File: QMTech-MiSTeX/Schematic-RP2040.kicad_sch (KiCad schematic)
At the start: 24 parts, among them J9 Conn_01x02, U1 W25Q128JVS, U2 RP2040, X1 X322512MSB4SI

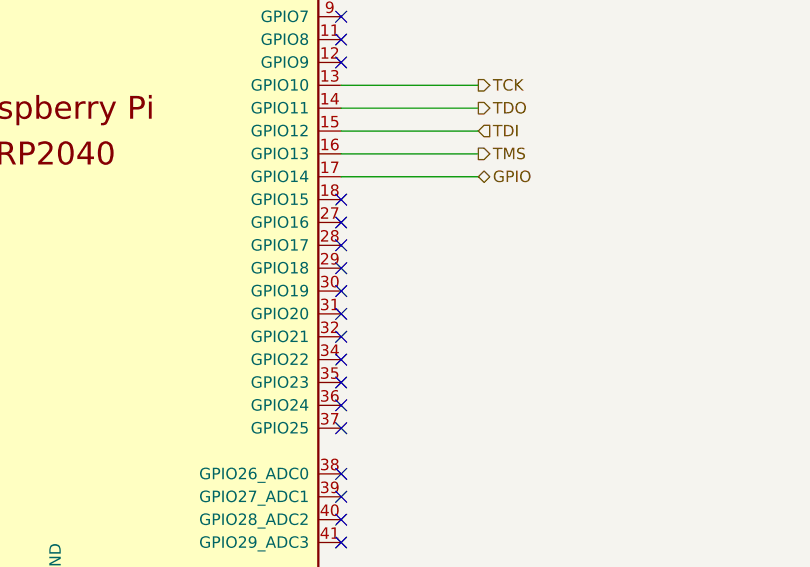
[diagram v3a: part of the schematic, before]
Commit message: add a power switch and break out and break out 4 more GPIOs on RP2040
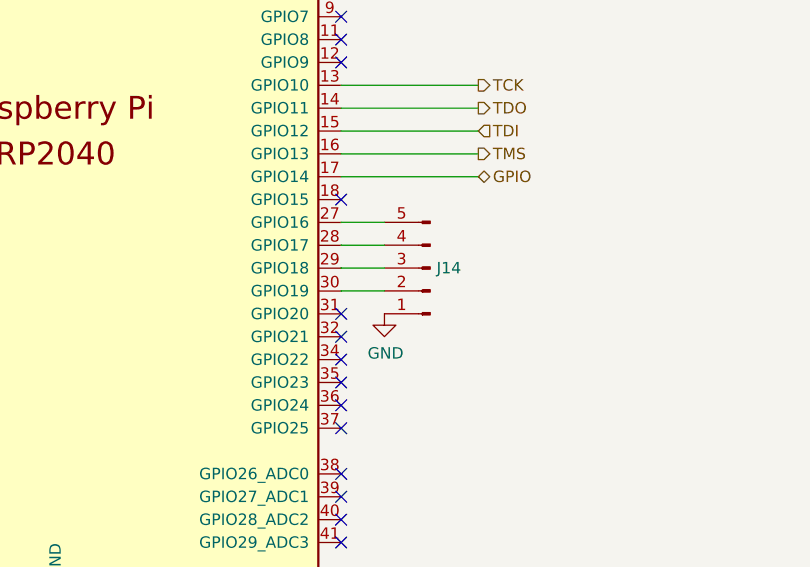
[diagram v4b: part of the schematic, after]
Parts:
- added J14: Conn_01x05_Pin, Connector_PinHeader_2.54mm:PinHeader_1x05_P2.54mm_Vertical, symbol Connector:Conn_01x05_Pin
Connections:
- net GND: now also J14.1 (Pin_1)
- net at U2.27 (GPIO16): now also J14.5 (Pin_5)
- net at U2.28 (GPIO17): now also J14.4 (Pin_4)
- net at U2.29 (GPIO18): now also J14.3 (Pin_3)
- net at U2.30 (GPIO19): now also J14.2 (Pin_2)
- no-connect marks 23 -> 19
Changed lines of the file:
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@@
   )
   (no_connect (at 186.4106 79.5782))
-  (no_connect (at 186.4106 117.6782))
   (no_connect (at 186.4106 89.7382))
   (no_connect (at 186.4106 92.2782))
@@
   (no_connect (at 186.4106 87.1982))
   (no_connect (at 186.4106 130.3782))
-  (no_connect (at 186.4106 120.2182))
-  (no_connect (at 186.4106 112.5982))
   (no_connect (at 186.4106 148.1582))
   (no_connect (at 186.4106 84.6582))
@@
   (no_connect (at 186.4106 143.0782))
   (no_connect (at 186.4106 110.0582))
-  (no_connect (at 186.4106 115.1382))
   (no_connect (at 186.4106 140.5382))
   (no_connect (at 186.4106 122.7582))
@@
     (stroke (width 0) (type default))
   )
+  (wire (pts (xy 191.2175 115.1242) (xy 186.4246 115.1242))
+    (stroke (width 0) (type default))
+  )
   (wire (pts (xy 237.2106 30.0482) (xy 225.7806 30.0482))
     (stroke (width 0) (type default))
@@
     (stroke (width 0) (type default))
   )
+  (wire (pts (xy 191.2175 117.6642) (xy 186.4246 117.6642))
+    (stroke (width 0) (type default))
+  )
+  (wire (pts (xy 186.4246 115.1242) (xy 186.4106 115.1382))
+    (stroke (width 0) (type default))
+  )
   (wire (pts (xy 202.9206 22.4282) (xy 202.9206 21.1582))
     (stroke (width 0) (type default))
@@
     (stroke (width 0) (type default))
   )
+  (wire (pts (xy 191.2175 120.2042) (xy 186.4246 120.2042))
+    (stroke (width 0) (type default))
+  )
   (wire (pts (xy 26.0096 84.0232) (xy 27.2796 84.0232))
     (stroke (width 0) (type default))
@@
     (stroke (width 0) (type default))
   )
+  (wire (pts (xy 186.4246 112.5842) (xy 186.4106 112.5982))
+    (stroke (width 0) (type default))
+  )
   (wire (pts (xy 122.9106 139.2682) (xy 108.9406 139.2682))
     (stroke (width 0) (type default))
@@
     (stroke (width 0) (type default))
   )
+  (wire (pts (xy 186.4246 120.2042) (xy 186.4106 120.2182))
+    (stroke (width 0) (type default))
+  )
   (wire (pts (xy 70.7136 113.3602) (xy 92.4306 113.3602))
     (stroke (width 0) (type default))
@@
     (stroke (width 0) (type default))
   )
+  (wire (pts (xy 186.4246 117.6642) (xy 186.4106 117.6782))
+    (stroke (width 0) (type default))
+  )
   (wire (pts (xy 49.2506 130.7592) (xy 53.4861 130.7592))
     (stroke (width 0) (type default))
@@
     (stroke (width 0) (type default))
   )
+  (wire (pts (xy 191.2175 112.5842) (xy 186.4246 112.5842))
+    (stroke (width 0) (type default))
+  )
   (wire (pts (xy 114.0206 22.4282) (xy 114.0206 21.1582))
     (stroke (width 0) (type default))
@@
     )
   )
+  (symbol (lib_id "power:GND") (at 191.2175 122.7442 0) (unit 1)
+    (in_bom yes) (on_board yes) (dnp no)
+    (property "Reference" "#PWR0154" (at 191.2175 129.0942 0)
+      (effects (font (size 1.27 1.27)) hide)
+    )
+    (property "Value" "GND" (at 191.3445 127.1384 0)
+      (effects (font (size 1.27 1.27)))
+    )
+    (property "Footprint" "" (at 191.2175 122.7442 0)
+      (effects (font (size 1.27 1.27)) hide)
+    )
+    (property "Datasheet" "" (at 191.2175 122.7442 0)
+      (effects (font (size 1.27 1.27)) hide)
+    )
+    (pin "1")
+    (instances
+      (project "QMTech-MiSTeX"
+        (path "/bf95850e-2fcb-4784-a603-f17fc357556b/6eb28fc4-fd96-4fb7-b136-67141c56dbda"
+          (reference "#PWR0154") (unit 1)
+        )
+      )
+    )
+  )
   (symbol (lib_id "jlcpcb-basic-mlcc-0402:100nF") (at 125.4506 24.9682 0) (unit 1)
     (in_bom yes) (on_board yes) (dnp no)
@@
         )
       )
+    )
+  )
+  (symbol (lib_id "Connector:Conn_01x05_Pin") (at 196.2975 117.6642 180) (unit 1)
+    (in_bom yes) (on_board yes) (dnp no) (fields_autoplaced)
+    (property "Reference" "J14" (at 197.0087 117.6642 0)
+      (effects (font (size 1.27 1.27)) (justify right))
+    )
+    (property "Value" "Conn_01x05_Pin" (at 197.0087 118.8763 0)
+      (effects (font (size 1.27 1.27)) (justify right) hide)
+    )
+    (property "Footprint" "Connector_PinHeader_2.54mm:PinHeader_1x05_P2.54mm_Vertical" (at 196.2975 117.6642 0)
+      (effects (font (size 1.27 1.27)) hide)
+    )
+    (property "Datasheet" "~" (at 196.2975 117.6642 0)
+      (effects (font (size 1.27 1.27)) hide)
+    )
+    (pin "2")
+    (pin "4")
+    (pin "3")
+    (pin "5")
+    (pin "1")
+    (instances
+      (project "QMTech-MiSTeX"
+        (path "/bf95850e-2fcb-4784-a603-f17fc357556b/6eb28fc4-fd96-4fb7-b136-67141c56dbda"
+          (reference "J14") (unit 1)
+        )
+      )

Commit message: silkscreen, schematic titles
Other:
- title: (none) -> RP2040 JTAG Programmer
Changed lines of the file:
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@@
 (kicad_sch (version 20230121) (generator eeschema)
   (paper "A4")
+  (title_block
+    (title "RP2040 JTAG Programmer")
+  )
   (junction (at 171.1706 36.3982) (diameter 0) (color 0 0 0 0)
   )

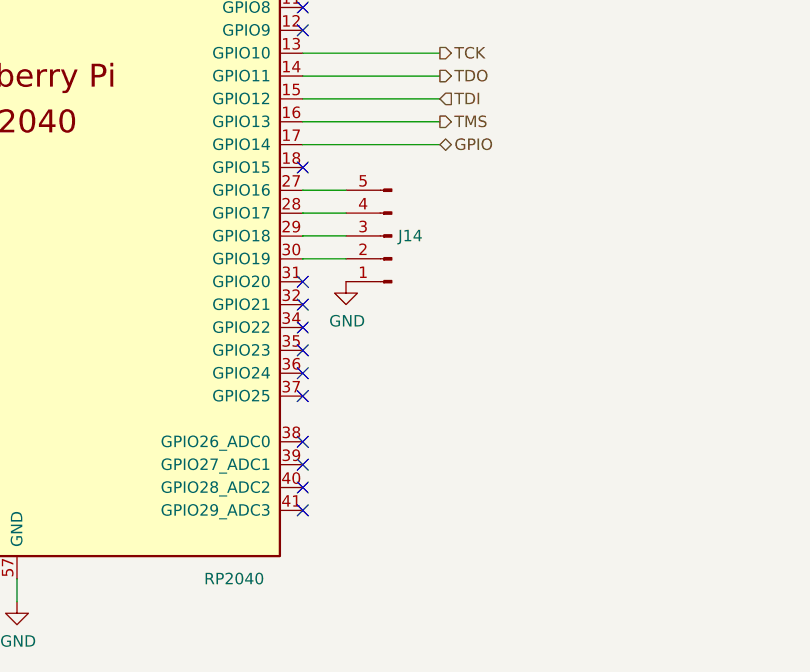
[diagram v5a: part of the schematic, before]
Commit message: add pin headers for buttons, add LED to RP2040, break out ADCs
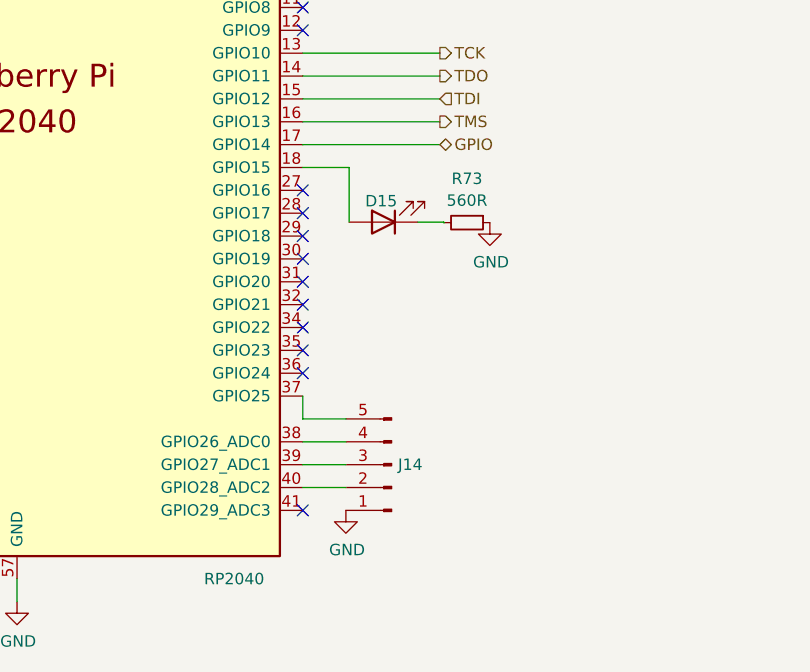
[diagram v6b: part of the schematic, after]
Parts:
- added D15: D_LED_0603_Green, LED_0603_1608Metric, symbol jlcpcb-basic-led:D_LED_0603_Green
- added R73: 560R, R_0603_1608Metric, symbol jlcpcb-basic-resistor-0603:560R
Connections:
- net GND: now also R73.1
- net at J14.2 (Pin_2): now also U2.40 (GPIO28_ADC2); no longer U2.30 (GPIO19)
- net at J14.3 (Pin_3): now also U2.39 (GPIO27_ADC1); no longer U2.29 (GPIO18)
- net at J14.4 (Pin_4): now also U2.38 (GPIO26_ADC0); no longer U2.28 (GPIO17)
- net at J14.5 (Pin_5): now also U2.37 (GPIO25); no longer U2.27 (GPIO16)
- net at U2.18 (GPIO15): now also D15.2 (A)
- new net: D15.1 (K), R73.2
- no-connect marks 19 -> 18
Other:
- moved on the sheet: J14
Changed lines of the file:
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@@
   (junction (at 180.0606 21.1582) (diameter 0) (color 0 0 0 0)
   )
+  (no_connect (at 186.4106 112.5982))
   (no_connect (at 186.4106 79.5782))
   (no_connect (at 186.4106 89.7382))
   (no_connect (at 186.4106 92.2782))
-  (no_connect (at 186.4106 135.4582))
-  (no_connect (at 186.4106 145.6182))
+  (no_connect (at 186.4106 115.1382))
   (no_connect (at 186.4106 127.8382))
   (no_connect (at 186.4106 82.1182))
@@
   (no_connect (at 186.4106 132.9182))
   (no_connect (at 186.4106 77.0382))
+  (no_connect (at 186.4246 120.2042))
   (no_connect (at 186.4106 125.2982))
-  (no_connect (at 186.4106 143.0782))
-  (no_connect (at 186.4106 110.0582))
-  (no_connect (at 186.4106 140.5382))
+  (no_connect (at 186.4106 117.6782))
   (no_connect (at 186.4106 122.7582))
   (wire (pts (xy 154.6606 155.7782) (xy 154.6606 158.3182))
     (stroke (width 0) (type default))
   )
+  (wire (pts (xy 186.4106 110.0582) (xy 191.5668 110.0582))
+    (stroke (width 0) (type default))
+  )
   (wire (pts (xy 108.9406 79.5782) (xy 122.9106 79.5782))
     (stroke (width 0) (type default))
@@
     (stroke (width 0) (type default))
   )
-  (wire (pts (xy 191.2175 115.1242) (xy 186.4246 115.1242))
+  (wire (pts (xy 191.2035 140.5382) (xy 186.4106 140.5382))
     (stroke (width 0) (type default))
   )
@@
     (stroke (width 0) (type default))
   )
-  (wire (pts (xy 191.2175 117.6642) (xy 186.4246 117.6642))
-    (stroke (width 0) (type default))
-  )
-  (wire (pts (xy 186.4246 115.1242) (xy 186.4106 115.1382))
+  (wire (pts (xy 191.2035 143.0782) (xy 186.4106 143.0782))
     (stroke (width 0) (type default))
   )
@@
     (stroke (width 0) (type default))
   )
+  (wire (pts (xy 202.1217 116.1853) (xy 202.0709 116.1853))
+    (stroke (width 0) (type default))
+  )
   (wire (pts (xy 225.7806 30.0482) (xy 214.3506 30.0482))
     (stroke (width 0) (type default))
@@
     (stroke (width 0) (type default))
   )
-  (wire (pts (xy 191.2175 120.2042) (xy 186.4246 120.2042))
+  (wire (pts (xy 191.2035 145.6182) (xy 186.4106 145.6182))
     (stroke (width 0) (type default))
   )
@@
     (stroke (width 0) (type default))
   )
-  (wire (pts (xy 186.4246 112.5842) (xy 186.4106 112.5982))
-    (stroke (width 0) (type default))
-  )
   (wire (pts (xy 122.9106 139.2682) (xy 108.9406 139.2682))
     (stroke (width 0) (type default))
@@
     (stroke (width 0) (type default))
   )
+  (wire (pts (xy 186.4106 135.4582) (xy 186.4106 137.9982))
+    (stroke (width 0) (type default))
+  )
   (wire (pts (xy 72.9996 56.0832) (xy 72.9996 57.3532))
     (stroke (width 0) (type default))
@@
     (stroke (width 0) (type default))
   )
+  (wire (pts (xy 202.0709 116.1288) (xy 199.1868 116.1288))
+    (stroke (width 0) (type default))
+  )
   (wire (pts (xy 171.1706 25.7302) (xy 161.3916 25.7302))
     (stroke (width 0) (type default))
@@
     (stroke (width 0) (type default))
   )
+  (wire (pts (xy 202.0709 116.1853) (xy 202.0709 116.1288))
+    (stroke (width 0) (type default))
+  )
   (wire (pts (xy 85.6996 78.9432) (xy 102.2096 78.9432))
     (stroke (width 0) (type default))
@@
     (stroke (width 0) (type default))
   )
-  (wire (pts (xy 186.4246 117.6642) (xy 186.4106 117.6782))
-    (stroke (width 0) (type default))
-  )
   (wire (pts (xy 49.2506 130.7592) (xy 53.4861 130.7592))
     (stroke (width 0) (type default))
@@
     (stroke (width 0) (type default))
   )
+  (wire (pts (xy 191.5668 110.0582) (xy 191.5668 116.1288))
+    (stroke (width 0) (type default))
+  )
   (wire (pts (xy 186.4106 64.3382) (xy 197.8406 64.3382))
     (stroke (width 0) (type default))
@@
     (stroke (width 0) (type default))
   )
-  (wire (pts (xy 191.2175 112.5842) (xy 186.4246 112.5842))
+  (wire (pts (xy 191.2035 137.9982) (xy 186.4106 137.9982))
     (stroke (width 0) (type default))
   )
@@
     )
   )
-  (symbol (lib_id "power:GND") (at 191.2175 122.7442 0) (unit 1)
+  (symbol (lib_id "power:GND") (at 191.2035 148.1582 0) (unit 1)
     (in_bom yes) (on_board yes) (dnp no)
-    (property "Reference" "#PWR0154" (at 191.2175 129.0942 0)
+    (property "Reference" "#PWR0154" (at 191.2035 154.5082 0)
       (effects (font (size 1.27 1.27)) hide)
     )
-    (property "Value" "GND" (at 191.3445 127.1384 0)
+    (property "Value" "GND" (at 191.3305 152.5524 0)
       (effects (font (size 1.27 1.27)))
     )
-    (property "Footprint" "" (at 191.2175 122.7442 0)
+    (property "Footprint" "" (at 191.2035 148.1582 0)
       (effects (font (size 1.27 1.27)) hide)
     )
-    (property "Datasheet" "" (at 191.2175 122.7442 0)
+    (property "Datasheet" "" (at 191.2035 148.1582 0)
       (effects (font (size 1.27 1.27)) hide)
     )
@@
     )
   )
+  (symbol (lib_id "power:GND") (at 207.2017 116.1853 0) (unit 1)
+    (in_bom yes) (on_board yes) (dnp no)
+    (property "Reference" "#PWR0198" (at 207.2017 122.5353 0)
+      (effects (font (size 1.27 1.27)) hide)
+    )
+    (property "Value" "GND" (at 207.3287 120.5795 0)
+      (effects (font (size 1.27 1.27)))
+    )
+    (property "Footprint" "" (at 207.2017 116.1853 0)
+      (effects (font (size 1.27 1.27)) hide)
+    )
+    (property "Datasheet" "" (at 207.2017 116.1853 0)
+      (effects (font (size 1.27 1.27)) hide)
+    )
+    (pin "1")
+    (instances
+      (project "QMTech-MiSTeX"
+        (path "/bf95850e-2fcb-4784-a603-f17fc357556b/6eb28fc4-fd96-4fb7-b136-67141c56dbda"
+          (reference "#PWR0198") (unit 1)
+        )
+      )
+    )
+  )
   (symbol (lib_id "power:GND") (at 180.0606 44.0064 0) (unit 1)
     (in_bom yes) (on_board yes) (dnp no)
@@
     )
   )
-  (symbol (lib_id "Connector:Conn_01x05_Pin") (at 196.2975 117.6642 180) (unit 1)
+  (symbol (lib_id "Connector:Conn_01x05_Pin") (at 196.2835 143.0782 180) (unit 1)
     (in_bom yes) (on_board yes) (dnp no) (fields_autoplaced)
-    (property "Reference" "J14" (at 197.0087 117.6642 0)
+    (property "Reference" "J14" (at 196.9947 143.0782 0)
       (effects (font (size 1.27 1.27)) (justify right))
     )
-    (property "Value" "Conn_01x05_Pin" (at 197.0087 118.8763 0)
+    (property "Value" "Conn_01x05_Pin" (at 196.9947 144.2903 0)
       (effects (font (size 1.27 1.27)) (justify right) hide)
     )
-    (property "Footprint" "Connector_PinHeader_2.54mm:PinHeader_1x05_P2.54mm_Vertical" (at 196.2975 117.6642 0)
+    (property "Footprint" "Connector_PinHeader_2.54mm:PinHeader_1x05_P2.54mm_Vertical" (at 196.2835 143.0782 0)
       (effects (font (size 1.27 1.27)) hide)
     )
-    (property "Datasheet" "~" (at 196.2975 117.6642 0)
+    (property "Datasheet" "~" (at 196.2835 143.0782 0)
       (effects (font (size 1.27 1.27)) hide)
     )
@@
     )
   )
+  (symbol (lib_id "jlcpcb-basic-resistor-0603:560R") (at 204.6617 116.1853 270) (unit 1)
+    (in_bom yes) (on_board yes) (dnp no) (fields_autoplaced)
+    (property "Reference" "R73" (at 204.6617 111.3044 90)
+      (effects (font (size 1.27 1.27)))
+    )
+    (property "Value" "560R" (at 204.6617 113.7286 90)
+      (effects (font (size 1.27 1.27)))
+    )
+    (property "Footprint" "R_0603_1608Metric" (at 204.6617 114.4073 90)
+      (effects (font (size 1.27 1.27)) hide)
+    )
+    (property "Datasheet" "https://datasheet.lcsc.com/szlcsc/Uniroyal-Elec-0603WAF5600T5E_C23204.pdf" (at 204.6617 116.1853 90)
+      (effects (font (size 1.27 1.27)) hide)
+    )
+    (property "LCSC" "C23204" (at 204.6617 116.1853 90)
+      (effects (font (size 1.27 1.27)) hide)
+    )
+    (pin "2")
+    (pin "1")
+    (instances
+      (project "QMTech-MiSTeX"
+        (path "/bf95850e-2fcb-4784-a603-f17fc357556b/6eb28fc4-fd96-4fb7-b136-67141c56dbda"
+          (reference "R73") (unit 1)
+        )
+      )
+    )
+  )
   (symbol (lib_id "jlcpcb-basic-mlcc-0402:100nF") (at 180.0606 24.9682 0) (unit 1)
     (in_bom yes) (on_board yes) (dnp no)
@@
         )
       )
+    )
+  )
+  (symbol (lib_id "jlcpcb-basic-led:D_LED_0603_Green") (at 195.3768 116.1288 180) (unit 1)
+    (in_bom yes) (on_board yes) (dnp no)
+    (property "Reference" "D15" (at 195.1228 113.792 0)
+      (effects (font (size 1.27 1.27)))
+    )
+    (property "Value" "D_LED_0603_Green" (at 196.9643 112.2497 0)
+      (effects (font (size 1.27 1.27)) hide)
+    )
+    (property "Footprint" "LED_0603_1608Metric" (at 195.3768 116.1288 0)
+      (effects (font (size 1.27 1.27)) hide)
+    )
+    (property "Datasheet" "https://datasheet.lcsc.com/szlcsc/Everlight-Elec-19-217-GHC-YR1S2-3T_C72043.pdf" (at 195.3768 116.1288 90)
+      (effects (font (size 1.27 1.27)) hide)
+    )
+    (property "LCSC" "C72043" (at 195.3768 116.1288 90)
+      (effects (font (size 1.27 1.27)) hide)
+    )
+    (pin "1")
+    (pin "2")
+    (instances
+      (project "QMTech-MiSTeX"
+        (path "/bf95850e-2fcb-4784-a603-f17fc357556b/6eb28fc4-fd96-4fb7-b136-67141c56dbda"
+          (reference "D15") (unit 1)
+        )
+      )

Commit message: Use yellow LED for RP2040, because green is out of stock
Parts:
- D15: value D_LED_0603_Green -> D_LED_0603_Yellow; LCSC C72043 -> C72038
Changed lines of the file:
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@@
       (effects (font (size 1.27 1.27)))
     )
-    (property "Value" "D_LED_0603_Green" (at 196.9643 112.2497 0)
+    (property "Value" "D_LED_0603_Yellow" (at 196.9643 112.2497 0)
       (effects (font (size 1.27 1.27)) hide)
     )
@@
       (effects (font (size 1.27 1.27)) hide)
     )
-    (property "LCSC" "C72043" (at 195.3768 116.1288 90)
+    (property "LCSC" "C72038" (at 195.3768 116.1288 90)
       (effects (font (size 1.27 1.27)) hide)
     )
